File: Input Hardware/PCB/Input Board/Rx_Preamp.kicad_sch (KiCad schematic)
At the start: 44 parts, among them U2 TSV994, U4 TSV994

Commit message: Redo this one
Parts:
- removed 15k, 15k1, 15k13, 15k14, 15k15, 15k16, 15k5, 15k6: R, symbol Device:R
- removed C13, C14, C23, C31, C32, C33, C34, C5: 1.8nf, symbol Device:C
- removed C15, C16, C24, C35, C36, C37, C38, C6: 1.8nF, symbol Device:C
- removed C?: 100n, Capacitor_SMD:C_0603_1608Metric, symbol Device:C
- removed R10, R11, R18, R19, R20, R21, R34, R35, R36, R37, R39, R4, R40, R41, R6: 1k, symbol Device:R
- removed U2, U4: TSV994, symbol Amplifier_Operational:TSV994
- removed U?: TSV994, symbol Amplifier_Operational:TLV9064
- removed U?: TLV9064, symbol Amplifier_Operational:TLV9064
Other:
- note removed: "OPAMP NOT ALWAYS STABLE"
- note removed: "×17.7 @1MHz Gain slightly less to preserve bandwidth"

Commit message: explosion 💥
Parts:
- added C29, C? (x7): 1.8nf, symbol Device:C
- added C30, C? (x7): 1.8nF, symbol Device:C
- added R14, R15, R? (x14): 1k, symbol Device:R
- added R? (x8): 15k, symbol Device:R
- added U17, U? (x7): TSV994, symbol Amplifier_Operational:TSV994
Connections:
- new net: C?.1, R?.2, U?.3 (+) (x7)
- new net: C?.1, R?.2 (x7)
- new net: R?.1, R?.1, U?.2 (-) (x7)
- new net: C29.1, R14.2, U17.3 (+)
- new net: R15.1, R?.1, U17.2 (-)
- new net: C30.1, R15.2
- new net 1.65V: R14.1, R?.1, R?.1, R?.1, R?.1, R?.1
- new net GND: C30.2, C?.2, C?.2, C?.2, C?.2, C?.2, C?.2, C?.2
- new net RXIN1: C29.2
- new net RXIN2: C?.2
- new net RXIN3: C?.2
- new net RXIN4: C?.2
- new net RXIN5: C?.2
- new net RXIN6: C?.2
- new net RXIN7: C?.2
- new net RXIN8: C?.2
- new net RXOUT1: R?.2, U17.1
- new net RXOUT2: R?.2, U?.1
- new net RXOUT3: R?.2, U?.1
- new net RXOUT4: R?.2, U?.1
- new net RXOUT5: R?.2, U?.1
- new net RXOUT6: R?.2, U?.1
- new net RXOUT7: R?.2, U?.1
- new net RXOUT8: R?.2, U?.1
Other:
- note added: "OPAMP NOT ALWAYS STABLE"
- note added: "×17.7 @1MHz Gain slightly less to preserve bandwidth"

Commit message: Modify preamp
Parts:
- removed C? (x7): 1.8nF, symbol Device:C
- removed C? (x7): 1.8nf, symbol Device:C
- removed R? (x14): 1k, symbol Device:R
- removed R? (x7): 15k, symbol Device:R
- removed U? (x7): TSV994, symbol Amplifier_Operational:TSV994
- added C? (x2): 100n, Capacitor_SMD:C_0603_1608Metric, symbol Device:C
- added C? (x14): 1.8n, Capacitor_SMD:C_0603_1608Metric, symbol Device:C
- added R? (x7): 15k, Resistor_SMD:R_0603_1608Metric, symbol Device:R
- added R? (x14): 1k, Resistor_SMD:R_0603_1608Metric, symbol Device:R
- added U? (x9): TSV994, symbol Amplifier_Operational:TSV994
- C29: value 1.8nf -> 1.8n; footprint (none) -> Capacitor_SMD:C_0603_1608Metric
- C30: value 1.8nF -> 1.8n; footprint (none) -> Capacitor_SMD:C_0603_1608Metric
- R14, R15, R?: footprint (none) -> Resistor_SMD:R_0603_1608Metric
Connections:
- net 1.65V: now also R?.1, R?.1, R?.1, R?.1, R?.1, R?.1, R?.1
- net GND: now also C?.2, C?.2, C?.2, C?.2, C?.2, C?.2, C?.2, C?.2, C?.2, U?.11 (V-), U?.11 (V-)
- net RXIN2: now also C?.2
- net RXIN3: now also C?.2
- net RXIN4: now also C?.2
- net RXIN5: now also C?.2
- net RXIN6: now also C?.2
- net RXIN7: now also C?.2
- net RXIN8: now also C?.2
- net RXOUT2: now also R?.2, U?.7
- net RXOUT3: now also R?.2, U?.8
- net RXOUT4: now also R?.2, U?.14
- net RXOUT5: now also R?.2, U?.1
- net RXOUT6: now also R?.2, U?.7
- net RXOUT7: now also R?.2, U?.8
- net RXOUT8: now also R?.2, U?.14
- new net: R?.1, R?.1, U?.2 (-)
- new net: C?.1, R?.2, U?.3 (+)
- new net: R?.1, R?.1, U?.9 (-) (x2)
- new net: R?.1, R?.1, U?.13 (-) (x2)
- new net: C?.1, R?.2 (x7)
- new net: C?.1, R?.2, U?.12 (+) (x2)
- new net: C?.1, R?.2, U?.5 (+) (x2)
- new net: R?.1, R?.1, U?.6 (-) (x2)
- new net: C?.1, R?.2, U?.10 (+) (x2)
- new net +3.3V: C?.1, C?.1, U?.4 (V+), U?.4 (V+)

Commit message: spices
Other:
- note added: "This shouldnt really be ground should it? should be 1.65V??"
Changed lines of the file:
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@@
+		)
+	)
+	(text "This shouldnt really be ground should it? should be 1.65V??\n"
+		(exclude_from_sim no)
+		(at 17.78 59.69 0)
+		(effects
+			(font
+				(size 1.27 1.27)
+			)
 		)
 	)

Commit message: adc bandpass amp and rootpage update
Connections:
- net +3.3V: no longer U?.4 (V+), U?.4 (V+)
- net GND: no longer U?.11 (V-), U?.11 (V-)
- net RXOUT2: now also U?.1; no longer U?.7
- net RXOUT3: now also U?.1; no longer U?.8
- net RXOUT4: now also U?.1; no longer U?.14
- net RXOUT6: now also U?.1; no longer U?.7
- net RXOUT7: now also U?.1; no longer U?.8
- net RXOUT8: now also U?.1; no longer U?.14
- net at R?.1, R?.1: now also U?.2 (-); no longer U?.9 (-) (x2)
- net at R?.1, R?.1: now also U?.2 (-); no longer U?.13 (-) (x2)
- net at C?.1, R?.2: now also U?.3 (+); no longer U?.12 (+) (x2)
- net at C?.1, R?.2: now also U?.3 (+); no longer U?.5 (+) (x2)
- net at R?.1, R?.1: now also U?.2 (-); no longer U?.6 (-) (x2)
- net at C?.1, R?.2: now also U?.3 (+); no longer U?.10 (+) (x2)
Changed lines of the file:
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@@
 		(effects
 			(font
-				(size 1.27 1.27)
+				(size 2.54 2.54)
+				(thickness 0.508)
+				(bold yes)
 			)
 		)
@@
 		(lib_id "Amplifier_Operational:TSV994")
 		(at 66.04 152.4 0)
-		(unit 5)
+		(unit 4)
 		(exclude_from_sim no)
 		(in_bom yes)
@@
 				(path "/198ad8d1-66e3-4deb-889c-1af2b81e67c3/e110e9b7-e557-4981-bab6-c28116ad040e/f2897f03-1c65-406d-938e-483190e13ecf"
 					(reference "U?")
-					(unit 5)
+					(unit 4)
 				)
 			)
@@
 		(lib_id "Amplifier_Operational:TSV994")
 		(at 64.77 87.63 0)
-		(unit 2)
+		(unit 1)
 		(exclude_from_sim no)
 		(in_bom yes)
@@
 				(path "/198ad8d1-66e3-4deb-889c-1af2b81e67c3/e110e9b7-e557-4981-bab6-c28116ad040e/f2897f03-1c65-406d-938e-483190e13ecf"
 					(reference "U?")
-					(unit 2)
+					(unit 1)
 				)
 			)
@@
 		(lib_id "Amplifier_Operational:TSV994")
 		(at 191.77 90.17 0)
-		(unit 2)
+		(unit 1)
 		(exclude_from_sim no)
 		(in_bom yes)
@@
 				(path "/198ad8d1-66e3-4deb-889c-1af2b81e67c3/e110e9b7-e557-4981-bab6-c28116ad040e/f2897f03-1c65-406d-938e-483190e13ecf"
 					(reference "U?")
-					(unit 2)
+					(unit 1)
 				)
 			)
@@
 		(lib_id "Amplifier_Operational:TSV994")
 		(at 255.27 41.91 0)
-		(unit 3)
+		(unit 1)
 		(exclude_from_sim no)
 		(in_bom yes)
@@
 				(path "/198ad8d1-66e3-4deb-889c-1af2b81e67c3/e110e9b7-e557-4981-bab6-c28116ad040e/f2897f03-1c65-406d-938e-483190e13ecf"
 					(reference "U?")
-					(unit 3)
+					(unit 1)
 				)
 			)
@@
 		(lib_id "Amplifier_Operational:TSV994")
 		(at 91.44 152.4 0)
-		(unit 5)
+		(unit 4)
 		(exclude_from_sim no)
 		(in_bom yes)
@@
 				(path "/198ad8d1-66e3-4deb-889c-1af2b81e67c3/e110e9b7-e557-4981-bab6-c28116ad040e/f2897f03-1c65-406d-938e-483190e13ecf"
 					(reference "U?")
-					(unit 5)
+					(unit 4)
 				)
 			)
@@
 		(lib_id "Amplifier_Operational:TSV994")
 		(at 255.27 91.44 0)
-		(unit 4)
+		(unit 1)
 		(exclude_from_sim no)
 		(in_bom yes)
@@
 				(path "/198ad8d1-66e3-4deb-889c-1af2b81e67c3/e110e9b7-e557-4981-bab6-c28116ad040e/f2897f03-1c65-406d-938e-483190e13ecf"
 					(reference "U?")
-					(unit 4)
+					(unit 1)
 				)
 			)
@@
 		(lib_id "Amplifier_Operational:TSV994")
 		(at 128.27 88.9 0)
-		(unit 4)
+		(unit 1)
 		(exclude_from_sim no)
 		(in_bom yes)
@@
 				(path "/198ad8d1-66e3-4deb-889c-1af2b81e67c3/e110e9b7-e557-4981-bab6-c28116ad040e/f2897f03-1c65-406d-938e-483190e13ecf"
 					(reference "U?")
-					(unit 4)
+					(unit 1)
 				)
 			)
@@
 		(lib_id "Amplifier_Operational:TSV994")
 		(at 128.27 39.37 0)
-		(unit 3)
+		(unit 1)
 		(exclude_from_sim no)
 		(in_bom yes)
@@
 				(path "/198ad8d1-66e3-4deb-889c-1af2b81e67c3/e110e9b7-e557-4981-bab6-c28116ad040e/f2897f03-1c65-406d-938e-483190e13ecf"
 					(reference "U?")
-					(unit 3)
+					(unit 1)
 				)
 			)

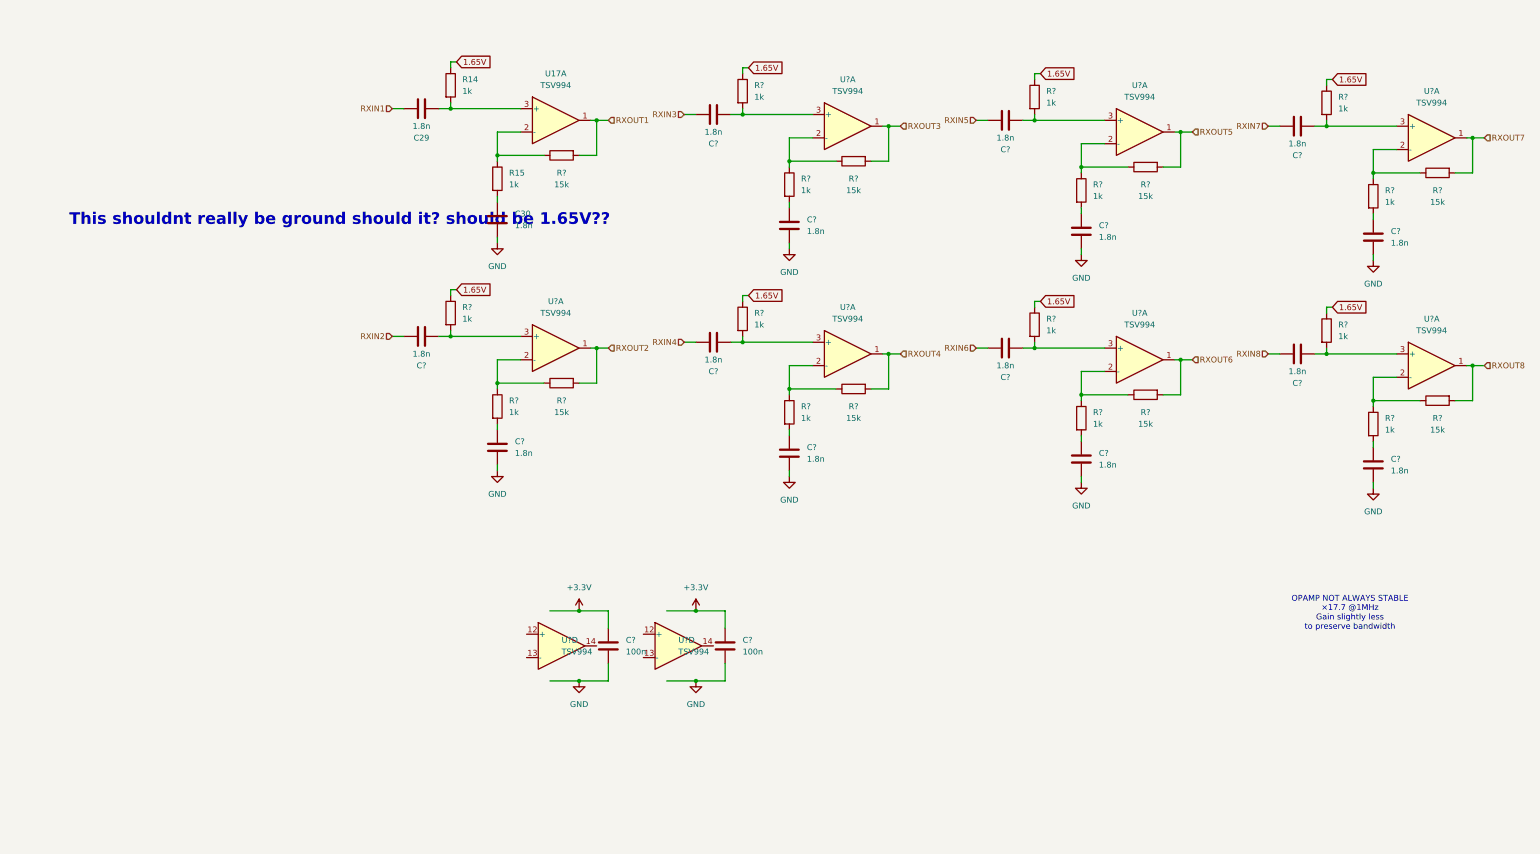
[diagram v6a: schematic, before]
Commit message: row amp fixes and spice fixes
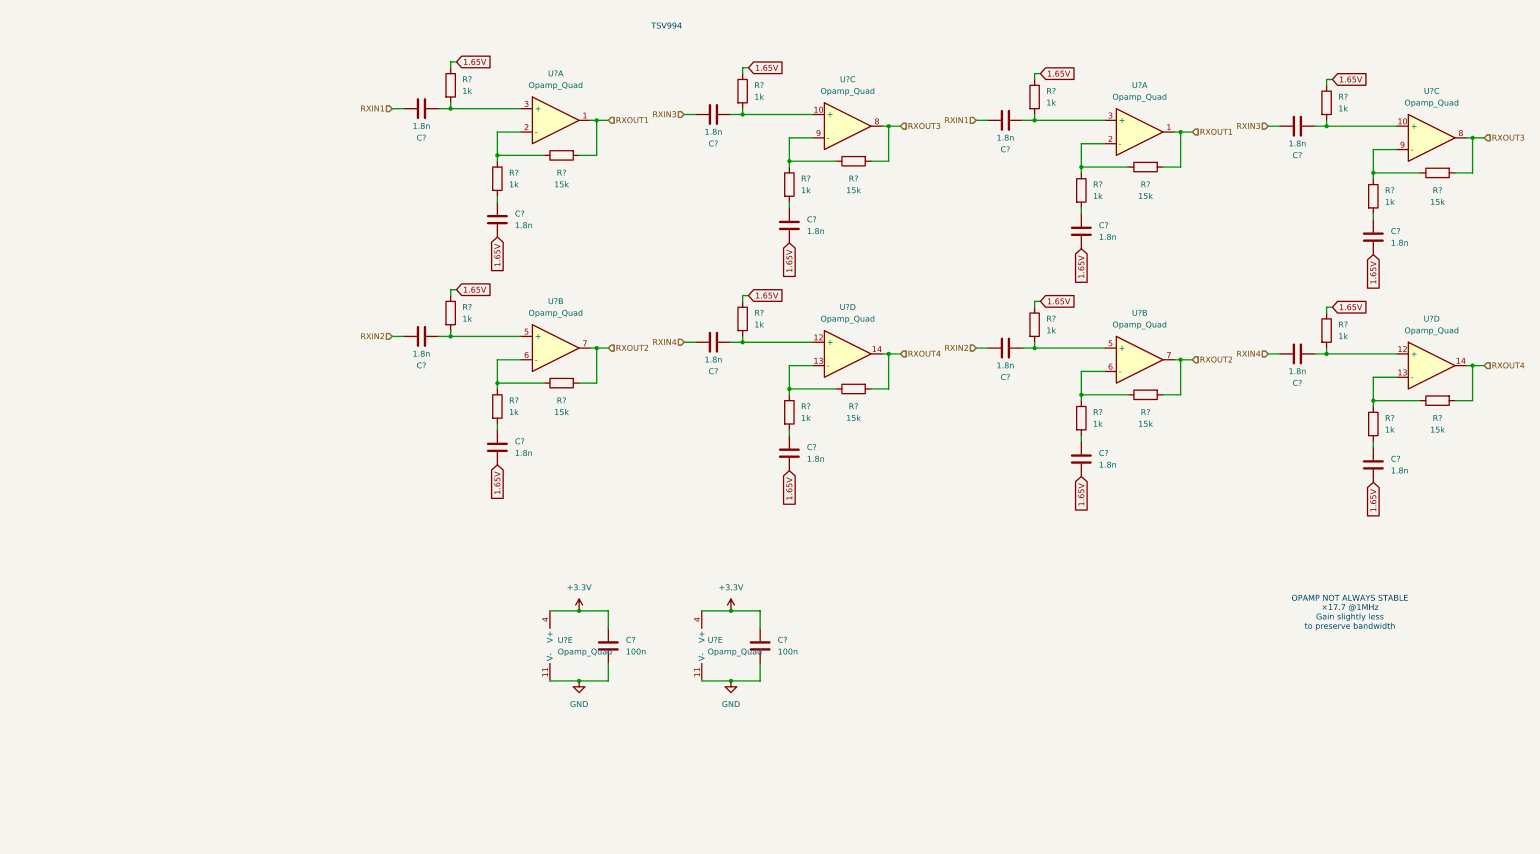
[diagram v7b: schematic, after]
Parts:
- removed C?: 100n, Capacitor_SMD:C_0603_1608Metric, symbol Device:C
- removed C? (x8): 1.8n, Capacitor_SMD:C_0603_1608Metric, symbol Device:C
- removed R? (x8): 1k, Resistor_SMD:R_0603_1608Metric, symbol Device:R
- removed R? (x4): 15k, Resistor_SMD:R_0603_1608Metric, symbol Device:R
- removed U17, U? (x9): TSV994, symbol Amplifier_Operational:TSV994
- added C? (x8): 1.8n, Capacitor_SMD:C_0603_1608Metric, symbol Device:C
- added C?: 100n, Capacitor_SMD:C_0603_1608Metric, symbol Device:C
- added R? (x4): 15k, Resistor_SMD:R_0603_1608Metric, symbol Device:R
- added R? (x8): 1k, Resistor_SMD:R_0603_1608Metric, symbol Device:R
- added U? (x10): Opamp_Quad, symbol Device:Opamp_Quad
- renumbered C29 to C?, C30 to C?, R14 to R?, R15 to R?
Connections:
- net +3.3V: now also C?.1, U?.4 (V+), U?.4 (V+)
- net 1.65V: now also C?.2, C?.2, C?.2, C?.2, C?.2, C?.2, C?.2, C?.2, R?.1, R?.1, R?.1, R?.1
- net GND: now also C?.2, U?.11 (V-), U?.11 (V-); no longer C?.2, C?.2, C?.2, C?.2
- net RXIN1: now also C?.2
- net RXIN2: now also C?.2
- net RXIN3: now also C?.2
- net RXIN4: now also C?.2
- net RXOUT1: now also R?.2, U?.1, U?.1
- net RXOUT2: now also R?.2, U?.7, U?.7
- net RXOUT3: now also R?.2, U?.8, U?.8
- net RXOUT4: now also R?.2, U?.14, U?.14
- net at R?.1, R?.1: now also U?.9 (-)
- net at C?.1, R?.2: now also U?.3 (+)
- net at C?.1, R?.2: now also U?.5 (+)
- net at R?.1, R?.1: now also U?.6 (-)
- net at R?.1, R?.1: now also U?.2 (-)
- net at R?.1, R?.1: now also U?.13 (-)
- net at C?.1, R?.2: now also U?.12 (+)
- net at C?.1, R?.2: now also U?.10 (+)
- new net: C?.1, R?.2, U?.5 (+)
- new net: R?.1, R?.1, U?.6 (-)
- new net: C?.1, R?.2 (x4)
- new net: R?.1, R?.1, U?.2 (-)
- new net: C?.1, R?.2, U?.3 (+)
- new net: C?.1, R?.2, U?.12 (+)
- new net: R?.1, R?.1, U?.9 (-)
- new net: R?.1, R?.1, U?.13 (-)
- new net: C?.1, R?.2, U?.10 (+)
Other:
- note added: "TSV994"
- note removed: "This shouldnt really be ground should it? should be 1.65V??"
